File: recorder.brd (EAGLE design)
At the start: 28.9 x 63.5 mm, 46 parts, among them M1 ELECTRET_MICROPHON-WM-61A, Q1 4.096MHz, T1 MMBT3904 NPN, U1 ISD15100

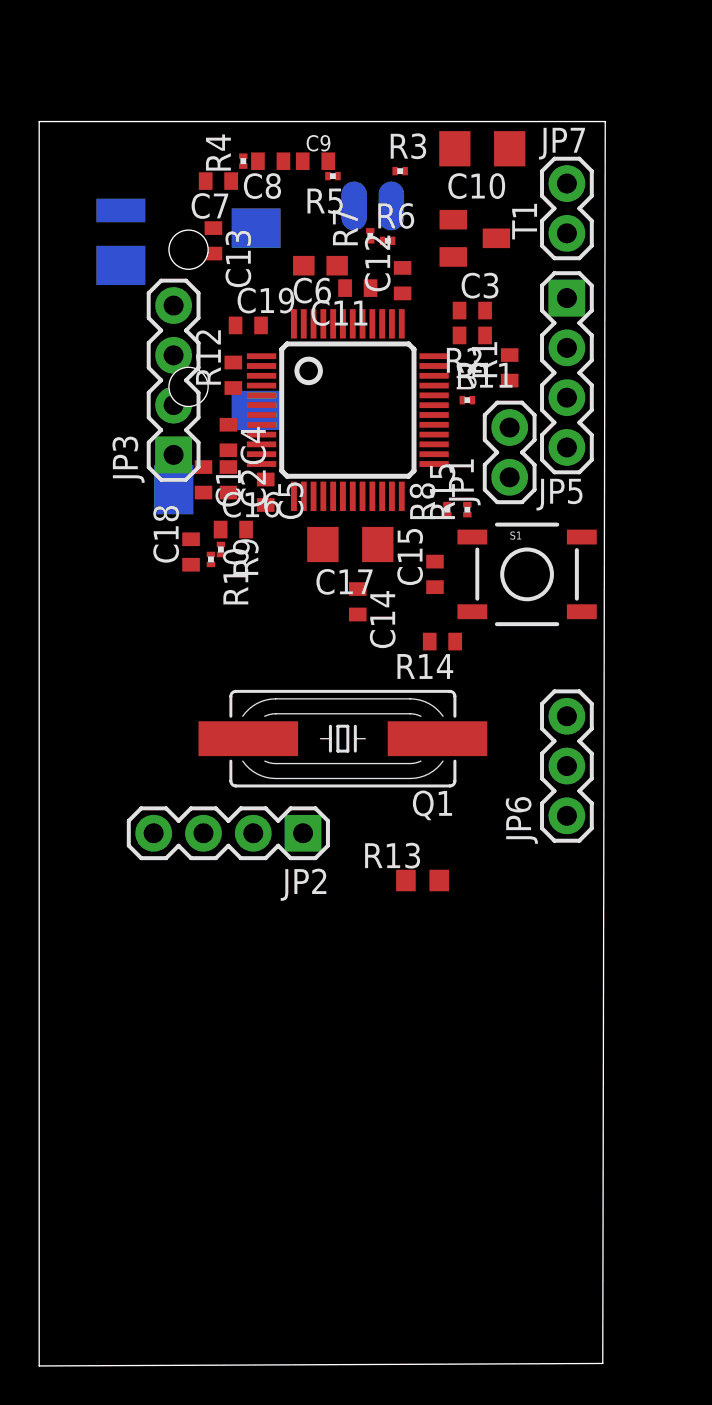
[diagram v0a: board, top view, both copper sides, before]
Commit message: rearranged dimensions of board
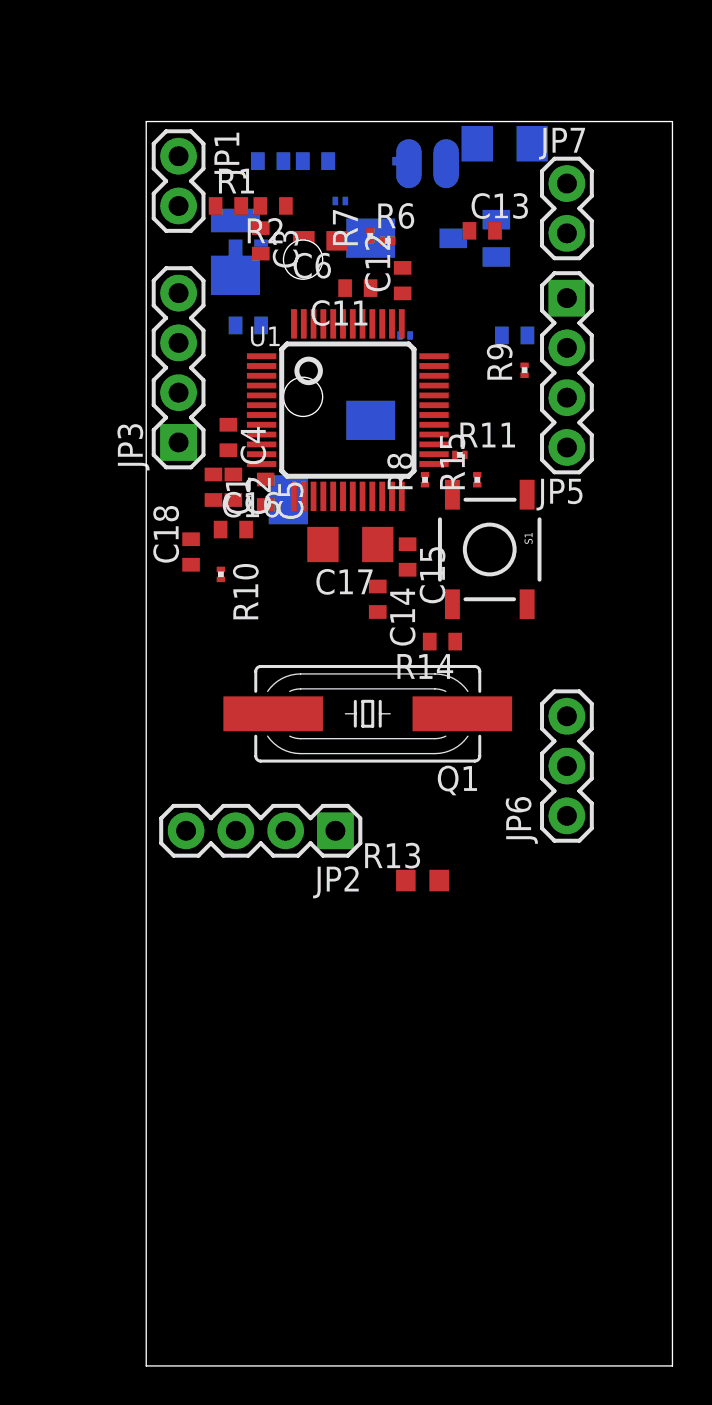
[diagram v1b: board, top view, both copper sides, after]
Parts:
- moved JP1 23.5 mm to (24.9, 74.4), turned to 270 degrees
- moved R9 18.0 mm to (42.5, 63.5), turned to 90 degrees
- moved C7 17.0 mm to (42.0, 65.3), flipped to the bottom
- moved R1 16.6 mm to (27.4, 71.9), turned to 0 degrees
- moved C13 13.7 mm to (40.4, 70.6), turned to 0 degrees
- moved R4 12.1 mm to (36.4, 65.3), flipped to the bottom, turned to 0 degrees
- moved R2 12.1 mm to (29.7, 71.9)
- moved C3 11.4 mm to (29.1, 70.1), turned to 270 degrees
- moved R12 6.52 mm to (28.4, 69.7), flipped to the bottom, turned to 180 degrees
- moved JP4 5.86 mm to (31.2, 72.6)
- moved M1 3.53 mm to (37.6, 74.0)
- moved R11 2.82 mm to (39.2, 59.2)
- moved S1 2.29 mm to (40.8, 54.4), turned to 270 degrees
- moved R8 1.90 mm to (37.5, 57.9)
- moved Q1 1.80 mm to (34.5, 46.0)
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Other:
- board size 28.9 x 63.5 mm -> 26.8 x 63.5 mm

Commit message: Began routing PCB traces. Almost finished but vias are not connected
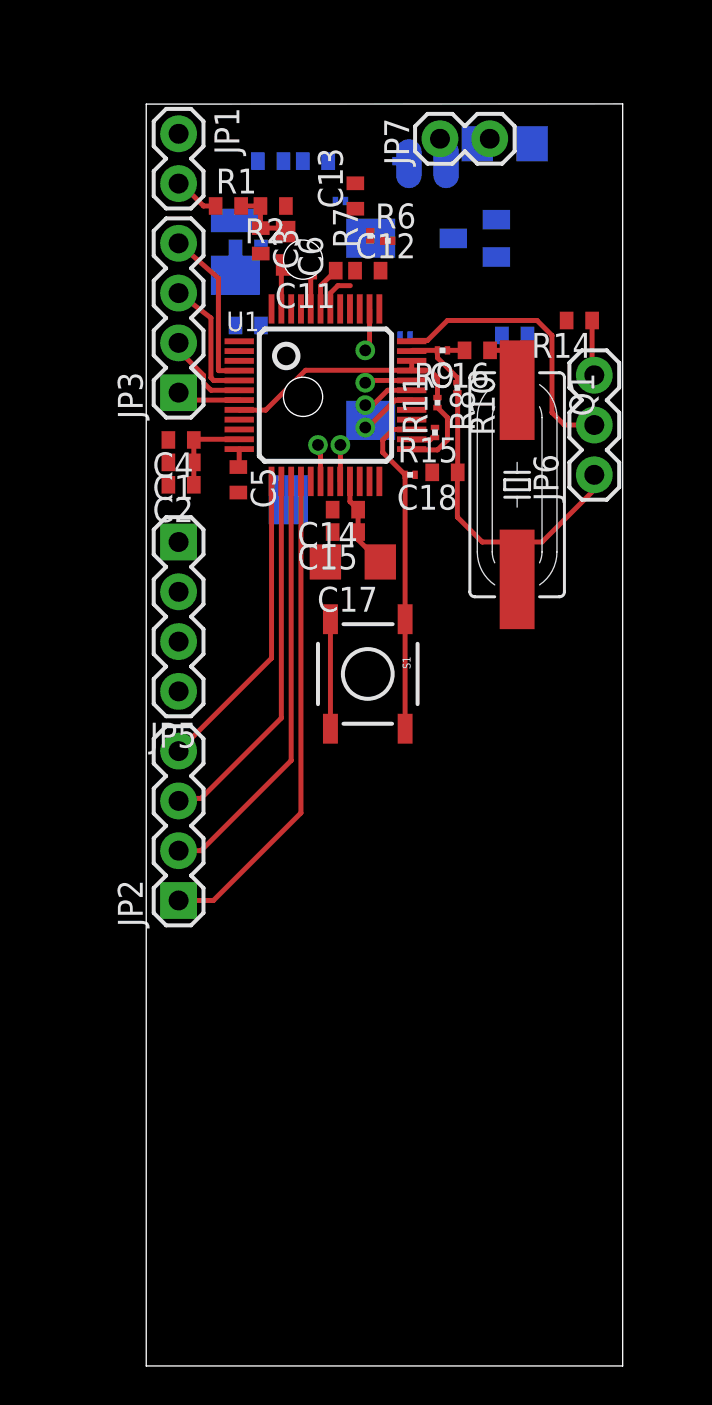
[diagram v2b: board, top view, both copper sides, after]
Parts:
- removed R13: 0 ohm, rcl:R0603
- moved JP5 23.4 mm to (24.9, 54.7)
- moved R14 17.8 mm to (45.3, 66.0)
- moved JP6 17.5 mm to (46.1, 58.2)
- moved C16 15.4 mm to (40.1, 64.5), turned to 180 degrees
- moved R10 15.4 mm to (39.1, 62.6)
- moved Q1 13.9 mm to (42.2, 57.7), turned to 270 degrees
- moved C18 13.6 mm to (38.5, 58.3), turned to 180 degrees
- moved S1 8.89 mm to (34.5, 48.0)
- moved JP2 8.76 mm to (24.9, 36.4), turned to 90 degrees
- moved JP7 6.87 mm to (38.2, 75.3), turned to 0 degrees
- moved C13 6.72 mm to (33.9, 72.4), turned to 90 degrees
- moved C14 4.86 mm to (33.4, 56.4), turned to 180 degrees
- moved R9 4.31 mm to (38.4, 64.5), turned to 180 degrees
- moved R8 3.99 mm to (38.1, 61.8), turned to 270 degrees
- moved R15 3.44 mm to (36.7, 58.2), turned to 0 degrees
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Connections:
- removed net AGND: C13.2, C19.2, C3.2, C7.2, JP1.1, R12.1, R13.1, R2.1, R5.1, R6.2, T1.E
- new net GND: C1.2, C13.2, C14.2, C15.2, C16.2, C17.2, C18.2, C19.2, C2.2, C3.2, C4.2, C5.2, C7.2, JP1.1, R11.2, R12.1, R14.2, R15.2, R2.1, R5.1, R6.2, T1.E, U1.10, U1.9
- net DGND: no longer C1.2, C14.2, C15.2, C16.2, C17.2, C18.2, C2.2, C4.2, C5.2, R11.2, R13.2, R14.2, R15.2, U1.10, U1.9
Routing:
- net MOSI: track 0.00 -> 25.0 mm
- net VCCD: track 0.00 -> 22.9 mm
- net SSB: track 0.00 -> 21.9 mm
- net SCLK: track 0.00 -> 19.1 mm
- net N$1: track 0.00 -> 17.9 mm
- net RESET: track 0.00 -> 16.9 mm
- net MISO: track 0.00 -> 15.7 mm
- net XTALIN: track 0.00 -> 14.3 mm
- net SDI: track 0.00 -> 8.47 mm
- net SCK: track 0.00 -> 6.63 mm
- net VCCD_PWM: track 0.00 -> 4.75 mm
- net WS: track 0.00 -> 4.54 mm
- net N$4: track 0.00 -> 3.91 mm
- net N$2: track 0.00 -> 3.82 mm
- net N$9: track 0.00 -> 3.47 mm
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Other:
- board size 26.8 x 63.5 mm -> 24.3 x 64.4 mm

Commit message: Finished layout of PCB board. DRC mostly clean other than drill requirements, which can be adjusted
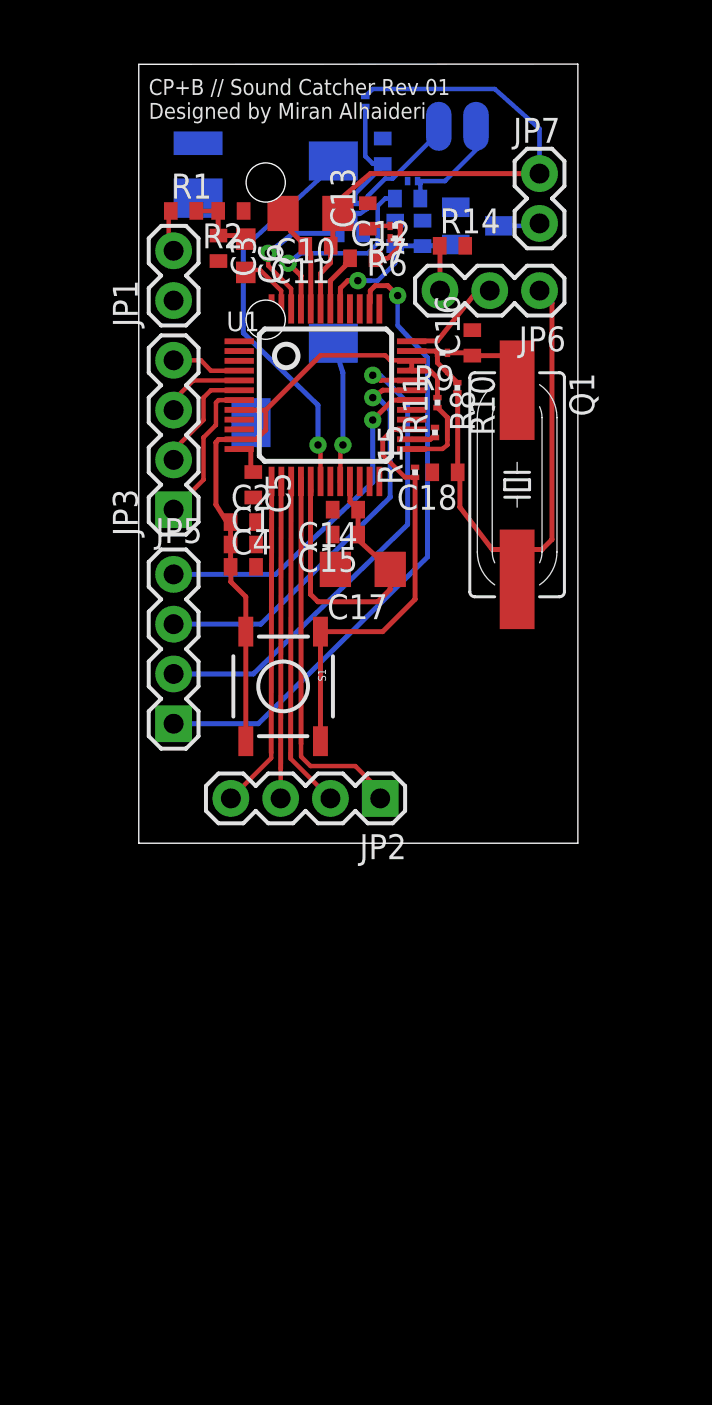
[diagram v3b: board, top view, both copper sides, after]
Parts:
- moved C7 11.6 mm to (35.3, 74.7), turned to 90 degrees
- moved JP2 11.5 mm to (35.2, 41.7), turned to 180 degrees
- moved C10 10.5 mm to (31.6, 71.5), flipped to the top
- moved JP6 9.80 mm to (43.3, 67.6), turned to 180 degrees
- moved JP5 9.27 mm to (24.6, 45.5), turned to 90 degrees
- moved R12 8.92 mm to (37.3, 70.5), turned to 270 degrees
- moved C19 8.84 mm to (35.9, 70.5), turned to 90 degrees
- moved JP1 8.51 mm to (24.6, 67.1), turned to 90 degrees
- moved R14 7.51 mm to (38.9, 69.8), turned to 0 degrees
- moved C4 7.21 mm to (28.2, 53.5), turned to 0 degrees
- moved R4 6.96 mm to (33.9, 71.8), turned to 270 degrees
- moved JP3 5.97 mm to (24.6, 56.4)
- moved C8 5.48 mm to (33.7, 70.5)
- moved JP7 5.38 mm to (43.3, 73.5), turned to 270 degrees
- moved C1 5.26 mm to (28.2, 54.6), turned to 0 degrees
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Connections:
- net N$11 renamed AUXOUT
- removed net DGND: U1.19
- net GND: now also U1.19
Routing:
- net GPIO0: track 2.20 -> 32.7 mm, vias 0 -> 1
- net VCCA: track 2.27 -> 28.3 mm
- net GPIO1: track 2.42 -> 25.1 mm
- net GPIO2: track 2.68 -> 20.8 mm
- net SPK+: track 1.91 -> 20.0 mm
- net GPIO3: track 2.95 -> 17.0 mm, vias 0 -> 1
- net VCCD_PWM: track 4.75 -> 16.3 mm
- net MIC-: track 0.00 -> 9.96 mm, vias 0 -> 1
- net VCCD: track 22.9 -> 32.4 mm
- net XTALIN: track 14.3 -> 5.23 mm
- net N$1: track 17.9 -> 26.5 mm
- net AUDOUT: track 0.00 -> 7.96 mm, vias 0 -> 1
- net MIC+: track 0.00 -> 7.22 mm, vias 0 -> 1
- net N$22: track 0.00 -> 6.86 mm
- net N$28: track 0.00 -> 6.19 mm
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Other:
- board size 24.3 x 64.4 mm -> 22.4 x 39.8 mm
- board text added: "CP+B // Sound Catcher Rev 01 Designed by Miran Alhaideri"

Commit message: spaced out component further for easier routing and to pass Sunstone DRC rules. Also, added VCC, GND 2-pin connector
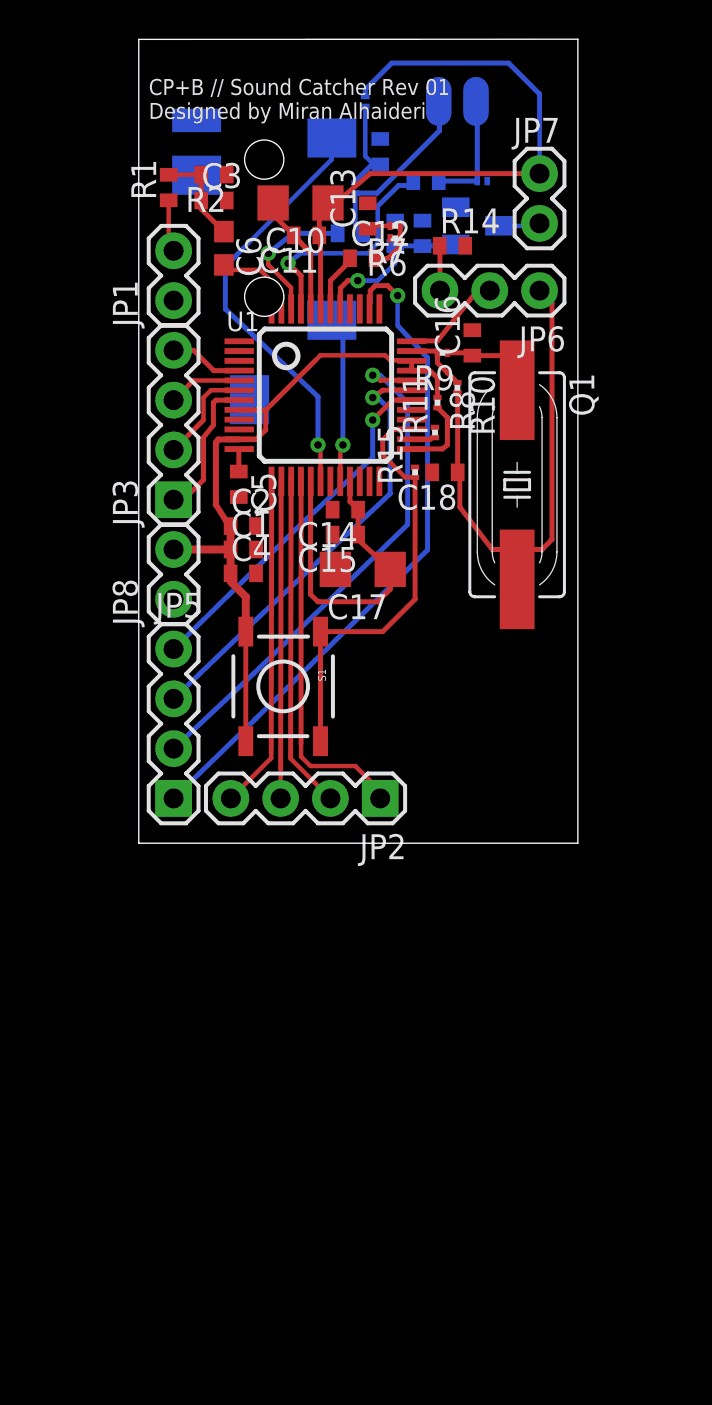
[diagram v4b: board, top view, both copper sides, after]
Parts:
- added JP8: M02PTH, SparkFun-Connectors:1X02
- moved JP5 3.81 mm to (24.6, 41.7)
- moved R5 3.56 mm to (40.4, 73.2), turned to 0 degrees
- moved C3 2.45 mm to (26.7, 72.2), turned to 0 degrees
- moved R2 2.05 mm to (26.7, 73.5)
- moved R1 1.42 mm to (24.4, 72.8), turned to 90 degrees
- moved C9 1.29 mm to (37.5, 73.2)
- moved M1 1.27 mm to (39.1, 77.2)
- moved C6 1.18 mm to (27.2, 69.7)
- moved JP4 1.17 mm to (29.3, 77.7)
- moved R4 1.04 mm to (33.9, 72.8)
- moved C11 0.79 mm to (31.4, 70.4)
- moved C5 0.74 mm to (28.0, 57.7)
- moved C10 0.74 mm to (31.1, 72.0)
- moved JP3 0.51 mm to (24.6, 56.9)
- moved C4 0.33 mm to (28.2, 53.1)
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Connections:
- net GND: now also JP8.1
- net VCCD: now also JP8.2
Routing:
- net VCCD: track 32.4 -> 35.6 mm
- net VCCA: track 28.3 -> 30.9 mm
- net SPK+: track 20.0 -> 21.8 mm
- net N$28: track 6.19 -> 4.55 mm
- net N$19: track 5.80 -> 7.42 mm
- net GPIO1: track 25.1 -> 26.6 mm
- net N$22: track 6.86 -> 8.35 mm
- net GPIO2: track 20.8 -> 22.2 mm
- net GPIO0: track 32.7 -> 34.0 mm
- net SPK-: track 7.19 -> 8.51 mm
- net MIC-: track 9.96 -> 11.3 mm
- net GPIO3: track 17.0 -> 17.8 mm
- net N$9: track 4.27 -> 5.05 mm
- net N$15: track 5.85 -> 5.24 mm
- net AUXIN: track 2.94 -> 3.50 mm
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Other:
- board size 22.4 x 39.8 mm -> 22.4 x 41 mm
